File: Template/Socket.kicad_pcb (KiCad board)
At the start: 2 copper layers, 220 x 65 mm, 13 parts, among them J1 CONNECTOR, J2 CONNECTOR, J3 CONNECTOR, J4 CONNECTOR, J5 CONNECTOR, J6 CONNECTOR

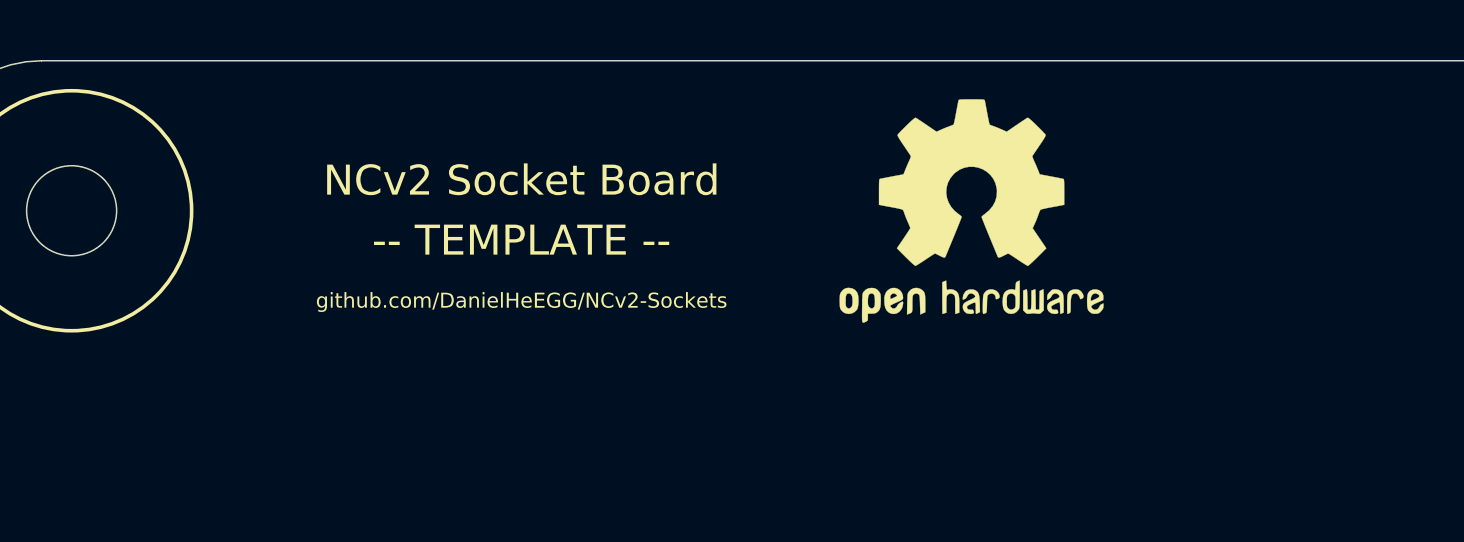
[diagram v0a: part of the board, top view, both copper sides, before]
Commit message: Increase silkscreen text size
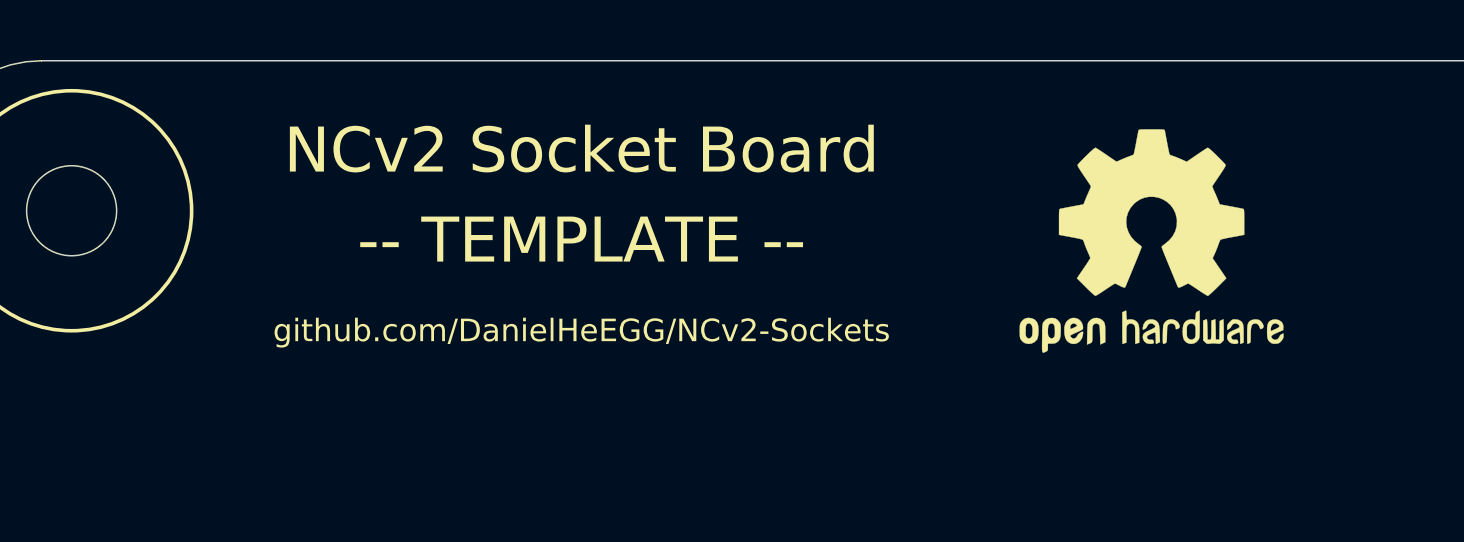
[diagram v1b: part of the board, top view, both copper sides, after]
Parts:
- moved REF** 6.08 mm to (86.0, 66.0)
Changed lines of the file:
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@@
   )
   (module Symbol:OSHW-Logo2_9.8x8mm_SilkScreen (layer F.Cu)
-    (at 80 65)
+    (at 86 66)
     (descr "Open Source Hardware Symbol")
     (tags "Logo Symbol OSHW")
@@
     (effects (font (size 0.5 0.5) (thickness 0.1)))
   )
-  (gr_text "-- TEMPLATE --" (at 65 66) (layer F.SilkS)
-    (effects (font (size 1 1) (thickness 0.15)))
-  )
-  (gr_text github.com/DanielHeEGG/NCv2-Sockets (at 65 68) (layer F.SilkS)
-    (effects (font (size 0.5 0.5) (thickness 0.1)))
-  )
-  (gr_text "NCv2 Socket Board" (at 65 64) (layer F.SilkS)
-    (effects (font (size 1 1) (thickness 0.15)))
+  (gr_text "-- TEMPLATE --" (at 67 66) (layer F.SilkS)
+    (effects (font (size 1.5 1.5) (thickness 0.2)))
+  )
+  (gr_text github.com/DanielHeEGG/NCv2-Sockets (at 67 69) (layer F.SilkS)
+    (effects (font (size 0.75 0.75) (thickness 0.1)))
+  )
+  (gr_text "NCv2 Socket Board" (at 67 63) (layer F.SilkS)
+    (effects (font (size 1.5 1.5) (thickness 0.2)))
   )
   (gr_line (start 261 60) (end 49 60) (layer Edge.Cuts) (width 0.05))

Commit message: Migrate to KiCAD 6
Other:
- net class Default removed
